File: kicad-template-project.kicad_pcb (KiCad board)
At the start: 6 copper layers, 50 x 50 mm, 92 parts, among them J1 Conn_ST_STDC14, J2 Conn_01x12, Q1 LMG2100R026, Q2 LMG2100R026, Q3 LMG2100R026, U1 MCS1823, U10 AD40xxBCPZ, U11 AD40xxBCPZ, U12 TPS54360DDA, U13 MIC5219YM5, U14 MIC5219YM5, U15 W25Q16JVSS, U2 MCS1823, U3 MCS1823, U4 ICE40UP5K-SG48ITR, U5 STM32L432KBUx, U6 SN65HVD230, U7 MIC5219YM5, U8 MLX90395xLW, U9 AD40xxBCPZ

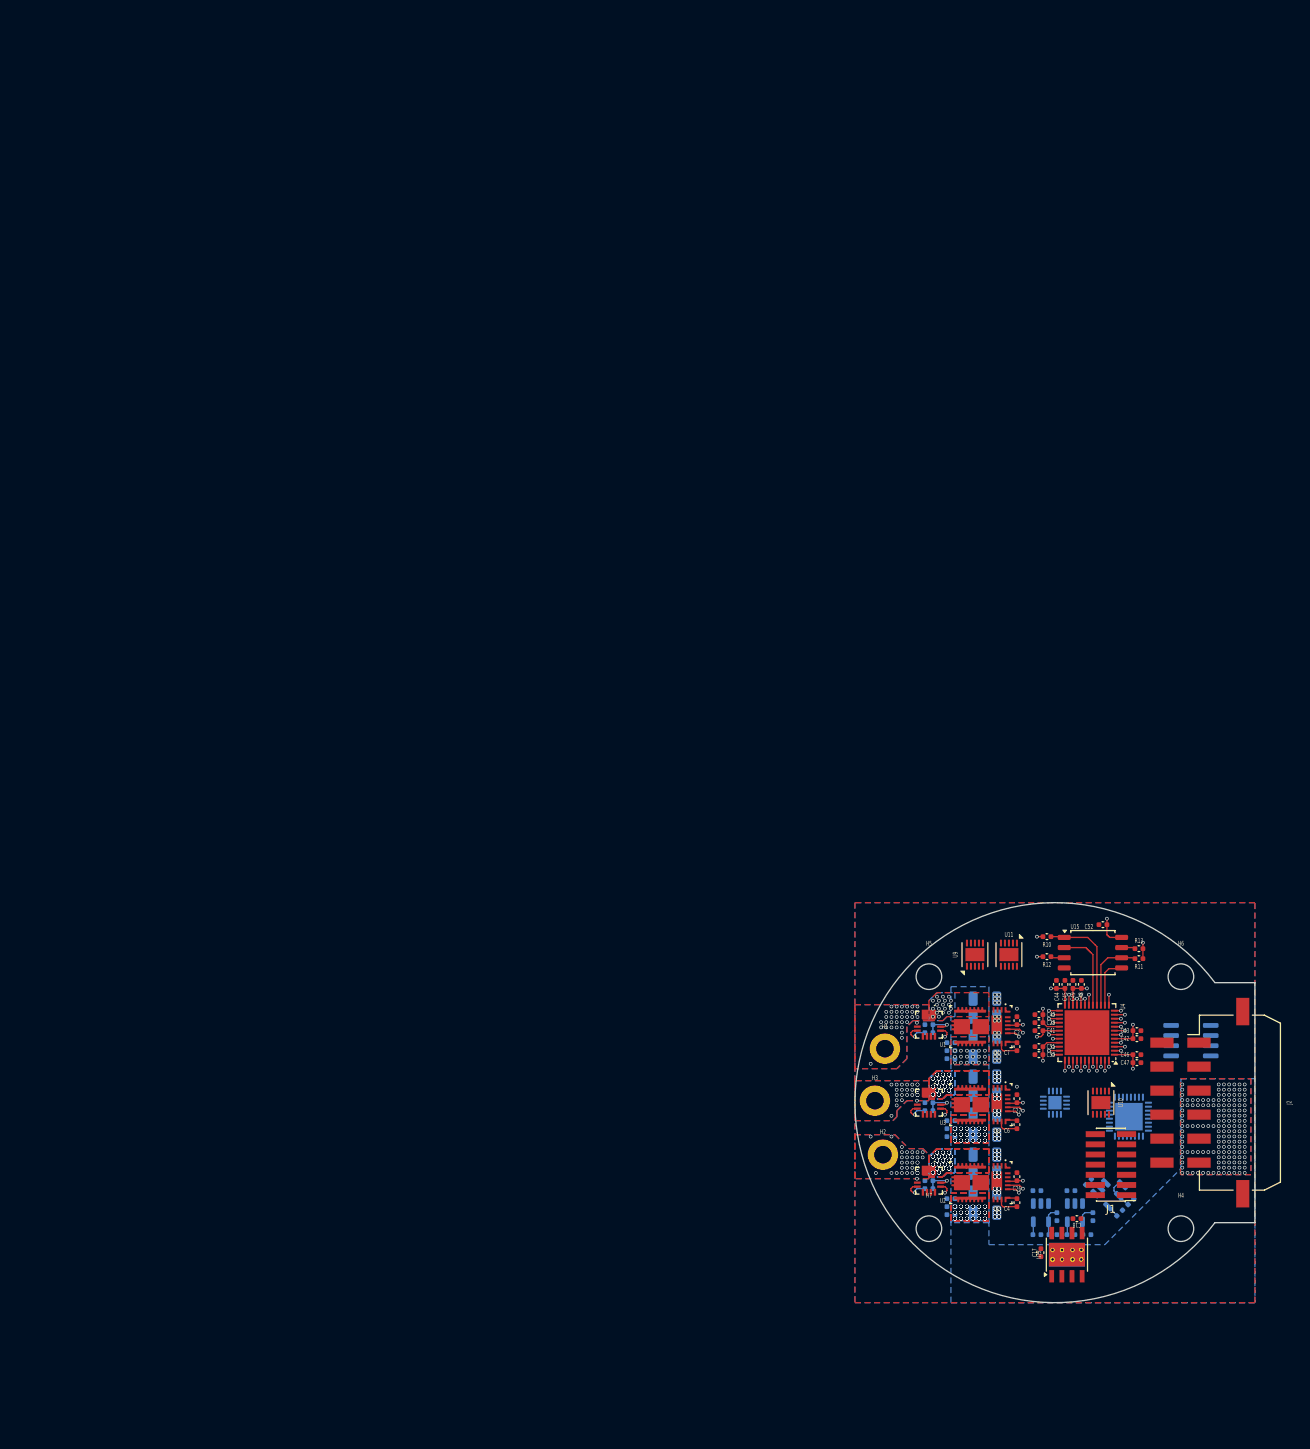
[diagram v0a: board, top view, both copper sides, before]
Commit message: fix: fleshignout schematic for mcu, fpga and mag + peripherals
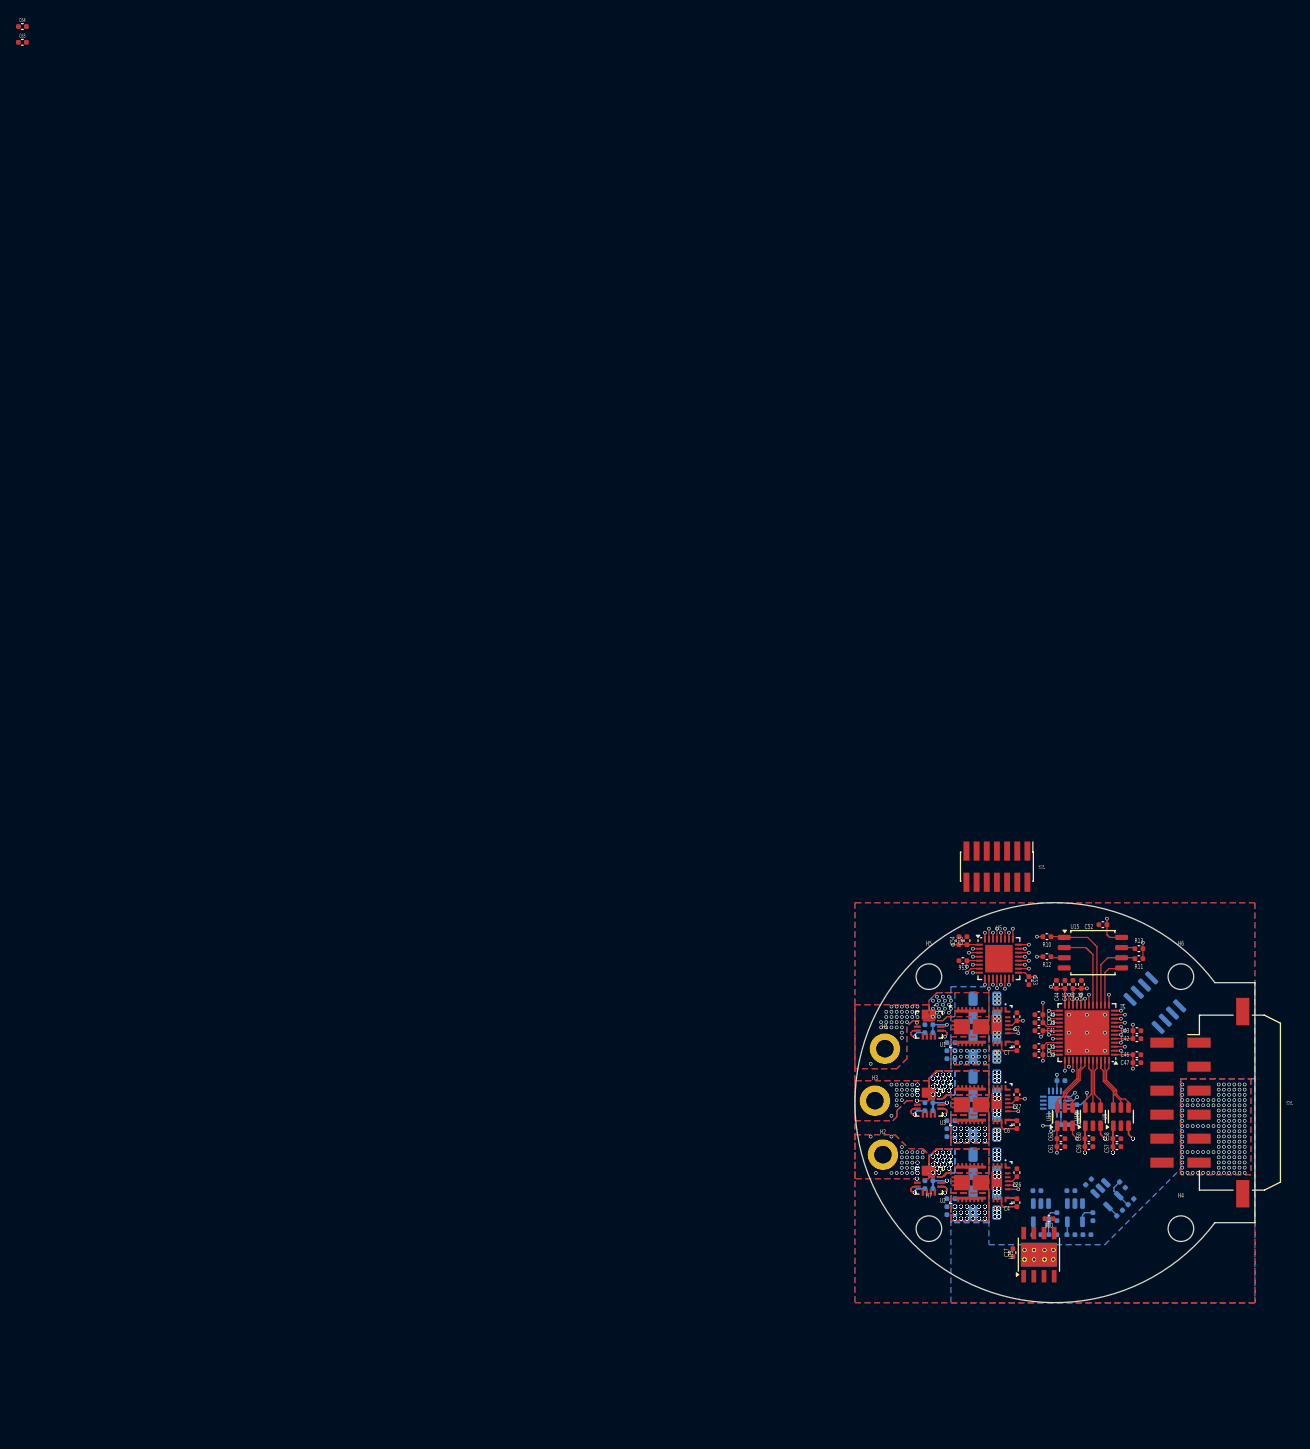
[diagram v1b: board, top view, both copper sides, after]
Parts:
- added C53: 100 nF, chenry-footprint-lib:C_0402, F.Cu at (126.8, 119.8)
- added C54: 4.7uF, chenry-footprint-lib:C_0402, F.Cu at (118.0, 114.8)
- added C55: 100 nF, chenry-footprint-lib:C_0402, F.Cu at (119.0, 114.8)
- added C56: 100 nF, chenry-footprint-lib:C_0402, F.Cu at (118.5, 117.2)
- added C57: 100 nF, chenry-footprint-lib:C_0402, F.Cu at (137.8, 140.5)
- added C58: 1 uF, chenry-footprint-lib:C_0402, F.Cu at (137.8, 139.5)
- added C59: 100 nF, chenry-footprint-lib:C_0402, F.Cu at (134.2, 140.5)
- added C60: 1 uF, chenry-footprint-lib:C_0402, F.Cu at (134.2, 139.5)
- added C61: 100 nF, chenry-footprint-lib:C_0402, F.Cu at (130.8, 140.5)
- added C62: 1 uF, chenry-footprint-lib:C_0402, F.Cu at (130.8, 139.5)
- added C63: 1 uF, chenry-footprint-lib:C_0402, B.Cu at (130.8, 132.2)
- added C64: 100 nF, chenry-footprint-lib:C_0402, F.Cu at (0.94, 0.48)
- added C65: 100 nF, chenry-footprint-lib:C_0402, F.Cu at (0.94, 2.46)
- added R14: 10K, chenry-footprint-lib:R_0402, B.Cu at (132.8, 135.8)
- added R15: 10K, chenry-footprint-lib:R_0402, B.Cu at (131.2, 137.8)
- U10, U11, U9: value AD40xxBCPZ -> ADCS7476; footprint Package_CSP:LFCSP-WD-10-1EP_3x3mm_P0.5mm_EP1.64x2.38mm -> Package_TO_SOT_SMD:SOT-23-6
- U5: moved to F.Cu
- U6: value SN65HVD230 -> ISO1044BD
- moved J1 39.9 mm to (122.8, 105.5), turned to -90 degrees
- moved U9 27.3 mm to (138.2, 136.8)
- moved U5 25.6 mm to (123.0, 117.0)
- moved U11 21.4 mm to (131.2, 136.8), turned to 90 degrees
- moved U6 6.54 mm to (142.5, 122.5), turned to -45 degrees
- moved C17 3.50 mm to (124.8, 153.8)
- moved C18 3.50 mm to (129.2, 149.5)
- moved U12 3.50 mm to (128.0, 154.0)
- moved U10 2.02 mm to (134.8, 136.8), turned to 90 degrees
- moved C2 0.50 mm to (125.2, 124.2)
- moved C26 0.50 mm to (125.2, 143.8)
- moved C27 0.50 mm to (125.2, 134.0)
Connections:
- Q1 pad 12: /PH0/PWM_HI -> /FPGA/PH0_PWM_HI
- Q1 pad 13: /PH0/PWM_LI -> /FPGA/PH0_PWM_LI
- Q2 pad 12: /PH1/PWM_HI -> /FPGA/PH1_PWM_HI
- Q2 pad 13: /PH1/PWM_LI -> /FPGA/PH1_PWM_LI
- Q3 pad 12: /PH2/PWM_HI -> /FPGA/PH2_PWM_HI
- Q3 pad 13: /PH2/PWM_LI -> /FPGA/PH2_PWM_LI
- R1 pad 1: /PH0/I_OCD -> /FPGA/PH0_OCD
- R2 pad 1: /PH1/I_OCD -> /FPGA/PH1_OCD
- R3 pad 1: /PH2/I_OCD -> /FPGA/PH2_OCD
- U1 pad 11: /PH0/ISNS -> /FPGA/ISNS1
- U1 pad 6: /PH0/I_OCD -> /FPGA/PH0_OCD
- U10 pad 1: unconnected-(U10-REF-Pad1) -> Net-(U10-VDD)
- U10 pad 2: unconnected-(U10-VDD-Pad2) -> GND
- U10 pad 3: unconnected-(U10-IN+-Pad3) -> /FPGA/ISNS1
- U10 pad 4: unconnected-(U10-IN--Pad4) -> /FPGA/ADC1_SCLK
- U10 pad 5: unconnected-(U10-GND-Pad5) -> /FPGA/ADC1_SDATA
- U10 pad 6: unconnected-(U10-CNV-Pad6) -> /FPGA/ADC1_CS
- U11 pad 1: unconnected-(U11-REF-Pad1) -> Net-(U11-VDD)
- U11 pad 2: unconnected-(U11-VDD-Pad2) -> GND
- U11 pad 3: unconnected-(U11-IN+-Pad3) -> /FPGA/ISNS2
- U11 pad 4: unconnected-(U11-IN--Pad4) -> /FPGA/ADC2_SCLK
- U11 pad 5: unconnected-(U11-GND-Pad5) -> /FPGA/ADC2_SDATA
- U11 pad 6: unconnected-(U11-CNV-Pad6) -> /FPGA/ADC2_CS
- U2 pad 11: /PH1/ISNS -> /FPGA/ISNS0
- U2 pad 6: /PH1/I_OCD -> /FPGA/PH1_OCD
- U3 pad 11: /PH2/ISNS -> /FPGA/ISNS2
- U3 pad 6: /PH2/I_OCD -> /FPGA/PH2_OCD
- U4 pad 19: unconnected-(U4B-IOB_29b-Pad19) -> /FPGA/SPI_CS
- U4 pad 20: unconnected-(U4B-IOB_25b_G3-Pad20) -> /FPGA/SPI_SCK
- U4 pad 21: unconnected-(U4B-IOB_23b-Pad21) -> /FPGA/SPI_MISO
- U4 pad 23: unconnected-(U4A-IOT_37a-Pad23) -> /FPGA/SPI_MOSI
- U4 pad 25: unconnected-(U4A-IOT_36b-Pad25) -> /FPGA/PH0_PWM_LI
- U4 pad 26: unconnected-(U4A-IOT_39a-Pad26) -> /FPGA/PH0_PWM_HI
- U4 pad 27: unconnected-(U4A-IOT_38b-Pad27) -> /FPGA/PH0_OCD
- U4 pad 28: unconnected-(U4A-IOT_41a-Pad28) -> /FPGA/PH2_OCD
- U4 pad 31: unconnected-(U4A-IOT_42b-Pad31) -> /FPGA/PH2_PWM_LI
- U4 pad 32: unconnected-(U4A-IOT_43a-Pad32) -> /FPGA/PH2_PWM_HI
- U4 pad 34: unconnected-(U4A-IOT_44b-Pad34) -> /FPGA/PH1_OCD
- U4 pad 35: unconnected-(U4A-IOT_46b_G0-Pad35) -> /FPGA/PH1_PWM_LI
- U4 pad 36: unconnected-(U4A-IOT_48b-Pad36) -> /FPGA/PH1_PWM_HI
- U4 pad 40: unconnected-(U4A-RGB1-Pad40) -> /FPGA/ADC2_CS
- U4 pad 41: unconnected-(U4A-RGB2-Pad41) -> /FPGA/ADC2_SDATA
- U4 pad 42: unconnected-(U4A-IOT_51a-Pad42) -> /FPGA/ADC2_SCLK
- U4 pad 43: unconnected-(U4A-IOT_49a-Pad43) -> /FPGA/ADC1_CS
- U4 pad 44: unconnected-(U4C-IOB_3b_G6-Pad44) -> /FPGA/ADC1_SDATA
- U4 pad 45: unconnected-(U4C-IOB_5b-Pad45) -> /FPGA/ADC1_SCLK
- U4 pad 46: unconnected-(U4C-IOB_0a-Pad46) -> /FPGA/ADC0_CS
- U4 pad 47: unconnected-(U4C-IOB_2a-Pad47) -> /FPGA/ADC0_SDATA
- U4 pad 48: unconnected-(U4C-IOB_4a-Pad48) -> /FPGA/ADC0_SCLK
- U5 pad 11: unconnected-(U5-PA5-Pad11) -> /FPGA/SPI_SCK
- U5 pad 12: unconnected-(U5-PA6-Pad12) -> /FPGA/SPI_MISO
- U5 pad 13: unconnected-(U5-PA7-Pad13) -> /FPGA/SPI_MOSI
- U5 pad 19: unconnected-(U5-PA9-Pad19) -> /MAG/I2C_SCL
- U5 pad 20: unconnected-(U5-PA10-Pad20) -> /MAG/I2C_SDA
- U5 pad 21: unconnected-(U5-PA11-Pad21) -> /CAN/CAN_RX
- U5 pad 22: unconnected-(U5-PA12-Pad22) -> /CAN/CAN_TX
- U6 pad 1: unconnected-(U6-D-Pad1) -> VDD_3V3
- U6 pad 2: unconnected-(U6-GND-Pad2) -> /CAN/CAN_TX
- U6 pad 3: unconnected-(U6-VCC-Pad3) -> /CAN/CAN_RX
- U6 pad 4: unconnected-(U6-R-Pad4) -> GND
- U6 pad 5: unconnected-(U6-Vref-Pad5) -> /CAN/ISO_CAN_L
- U6 pad 6: unconnected-(U6-CANL-Pad6) -> /CAN/ISO_CAN_H
- U6 pad 7: unconnected-(U6-CANH-Pad7) -> ISO_GND
- U6 pad 8: unconnected-(U6-Rs-Pad8) -> ISO_3V3
- U8 pad 1: unconnected-(U8-INT-Pad1) -> /MAG/MAG_INT
- U8 pad 11: unconnected-(U8-A1-Pad11) -> GND
- U8 pad 12: unconnected-(U8-A0-Pad12) -> GND
- U8 pad 2: unconnected-(U8-~{CS}-Pad2) -> VDD_3V3
- U8 pad 3: unconnected-(U8-SCLK-Pad3) -> /MAG/I2C_SCL
- U8 pad 5: unconnected-(U8-MOSI-Pad5) -> /MAG/I2C_SDA
- U8 pad 6: unconnected-(U8-MISO-Pad6) -> GND
- U8 pad 7: unconnected-(U8-INT/TRG-Pad7) -> /MAG/MAG_TRIG
- U9 pad 1: unconnected-(U9-REF-Pad1) -> Net-(U9-VDD)
- U9 pad 2: unconnected-(U9-VDD-Pad2) -> GND
- U9 pad 3: unconnected-(U9-IN+-Pad3) -> /FPGA/ISNS0
- U9 pad 4: unconnected-(U9-IN--Pad4) -> /FPGA/ADC0_SCLK
- U9 pad 5: unconnected-(U9-GND-Pad5) -> /FPGA/ADC0_SDATA
- U9 pad 6: unconnected-(U9-CNV-Pad6) -> /FPGA/ADC0_CS
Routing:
- net /FPGA/PH1_OCD: track 0.00 -> 42.2 mm, vias 0 -> 3
- net /MAG/I2C_SDA: track 0.00 -> 38.3 mm, vias 0 -> 2
- net /FPGA/ISNS0: track 0.00 -> 37.5 mm, vias 0 -> 5
- net /FPGA/ISNS1: track 0.00 -> 37.1 mm, vias 0 -> 3
- net /FPGA/PH2_OCD: track 0.00 -> 34.2 mm, vias 0 -> 3
- net /MAG/I2C_SCL: track 0.00 -> 30.1 mm, vias 0 -> 2
- net /FPGA/ISNS2: track 0.00 -> 29.1 mm, vias 0 -> 3
- net /FPGA/PH0_OCD: track 0.00 -> 23.4 mm, vias 0 -> 2
- net /FPGA/PH1_PWM_LI: track 0.00 -> 23.0 mm, vias 0 -> 2
- net /FPGA/PH1_PWM_HI: track 0.00 -> 22.8 mm, vias 0 -> 2
- net VDD_3V3: track 41.6 -> 64.1 mm, vias 12 -> 20
- net /FPGA/SPI_SCK: track 0.00 -> 14.9 mm, vias 0 -> 2
- net /FPGA/SPI_MISO: track 0.00 -> 14.5 mm, vias 0 -> 2
- net /FPGA/PH2_PWM_LI: track 0.00 -> 14.4 mm, vias 0 -> 2
- net /FPGA/PH2_PWM_HI: track 0.00 -> 14.0 mm, vias 0 -> 2
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
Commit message: fix: adjusting positioning of programmign header
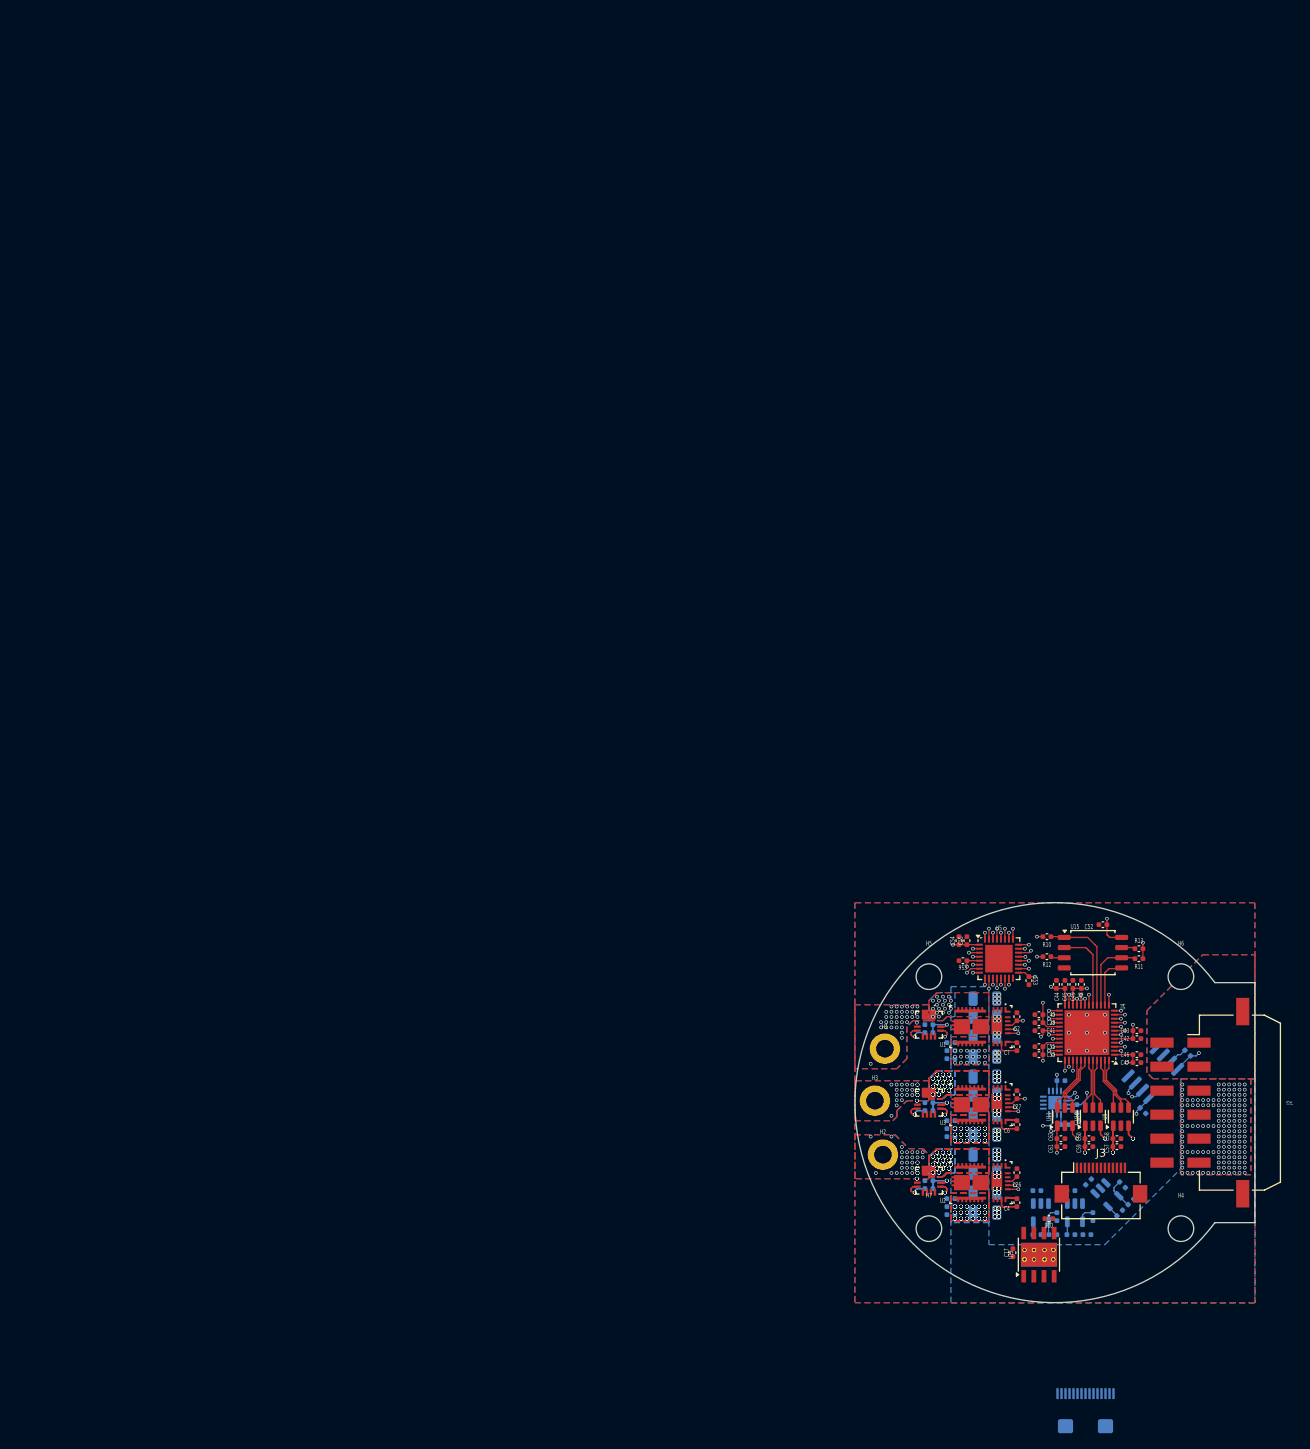
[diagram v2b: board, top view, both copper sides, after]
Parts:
- added J3: Conn_01x13, Connector_FFC-FPC:Hirose_FH12-13S-0.5SH_1x13-1MP_P0.50mm_Horizontal, F.Cu at (135.8, 145.0)
- C64, C65: moved to B.Cu
- J1: footprint Connector_PinHeader_1.27mm:PinHeader_2x07_P1.27mm_Vertical_SMD -> Connector_FFC-FPC:Molex_502231-1500_1x15-1SH_P0.5mm_Vertical; moved to B.Cu
- moved C64 194.1 mm to (146.6, 128.8), turned to 135 degrees
- moved C65 193.5 mm to (141.0, 136.0), turned to -45 degrees
- moved J1 67.8 mm to (133.8, 172.4), turned to 180 degrees
- moved U6 8.75 mm to (142.2, 131.2), turned to 45 degrees
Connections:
- C64 pad 2: GND -> ISO_GND
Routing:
- net /CAN/CAN_TX: track 1.31 -> 33.5 mm, vias 1 -> 2
- net /CAN/CAN_RX: track 0.81 -> 33.0 mm, vias 1 -> 2
- net ISO_3V3: track 0.00 -> 3.55 mm, vias 0 -> 1
- net VDD_3V3: track 64.1 -> 66.8 mm, vias 20 -> 21
- net ISO_GND: track 0.00 -> 2.42 mm
- added copper zone on B.Cu, net (none)
- added copper zone on F.Cu, net (none)
- added copper zone on In1.Cu, net (none)
- added copper zone on In2.Cu, net (none)
- added copper zone on In3.Cu, net (none)
- added copper zone on In4.Cu, net (none)
